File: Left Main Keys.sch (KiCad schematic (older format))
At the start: 6 parts

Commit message: Schematic completed first draft
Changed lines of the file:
@@
 $Descr A4 11693 8268
 encoding utf-8
-Sheet 9 12
+Sheet 11 18
 Title ""
 Date ""
@@
 Entry Wire Line
 	6150 6500 6250 6600
-Wire Bus Line
-	6350 6200 6250 6200
-Wire Bus Line
-	6350 6100 6250 6100
-Connection ~ 6350 6100
-Wire Bus Line
-	6350 6100 6350 6200
-Wire Bus Line
-	6350 6000 6250 6000
-Connection ~ 6350 6000
-Wire Bus Line
-	6350 6000 6350 6100
-Wire Bus Line
-	6350 5900 6250 5900
-Connection ~ 6350 5900
-Wire Bus Line
-	6350 5900 6350 6000
-Wire Bus Line
-	6350 5800 6250 5800
-Connection ~ 6350 5800
-Wire Bus Line
-	6350 5800 6350 5900
-Wire Bus Line
-	6350 5700 6250 5700
-Connection ~ 6350 5700
-Wire Bus Line
-	6350 5700 6350 5800
-Wire Bus Line
-	6350 5600 6250 5600
-Connection ~ 6350 5600
-Wire Bus Line
-	6350 5600 6350 5700
-Wire Bus Line
-	6350 5500 6250 5500
-Connection ~ 6350 5500
-Wire Bus Line
-	6350 5500 6350 5600
 Entry Wire Line
 	3200 2900 3300 2800
@@
 Entry Wire Line
 	7100 3200 7200 3100
-Wire Bus Line
-	6250 6300 6450 6300
-Wire Bus Line
-	6250 6400 6450 6400
-Wire Bus Line
-	6250 6500 6450 6500
-Wire Bus Line
-	6250 6600 6450 6600
-Connection ~ 6450 6300
-Connection ~ 6450 6400
-Wire Bus Line
-	6450 6400 6450 6300
-Connection ~ 6450 6500
-Wire Bus Line
-	6450 6500 6450 6400
-Wire Bus Line
-	6450 6600 6450 6500
 Text HLabel 10100 1150 0    50   Input ~ 0
 SHIFT_0_DATA_IN
 Wire Wire Line
 	10100 1150 10600 1150
-Wire Bus Line
-	6350 4300 6350 5500
 Wire Wire Line
 	1000 1150 1400 1150
@@
 Wire Wire Line
 	9350 1250 9350 3500
-Wire Bus Line
-	3200 4400 6250 4400
 Wire Wire Line
 	1500 1050 4100 1050
@@
 Wire Wire Line
 	8500 3500 9350 3500
-Wire Bus Line
-	6450 4300 6450 6300
 $Sheet
 S 4650 4550 1250 2050
@@
 Wire Wire Line
 	1500 4650 4650 4650
-Wire Bus Line
-	7100 4300 6450 4300
 Wire Wire Line
 	7200 2800 7400 2800
@@
 	5200 3500 5400 3500
 Wire Bus Line
-	5100 4300 6350 4300
-Wire Bus Line
-	7100 2900 7100 4300
-Wire Bus Line
-	5100 2900 5100 4300
-Wire Bus Line
-	3200 2900 3200 4400
-Wire Bus Line
-	6250 4400 6250 5400
+	6250 4350 5100 4350
+Connection ~ 5100 4350
+Wire Bus Line
+	5100 4350 3200 4350
+Wire Bus Line
+	6250 4350 7100 4350
+Wire Bus Line
+	7100 2900 7100 4350
+Wire Bus Line
+	3200 2900 3200 4350
+Wire Bus Line
+	5100 2900 5100 4350
+Wire Bus Line
+	6250 4350 6250 6600
+Connection ~ 6250 4350
 $EndSCHEMATC

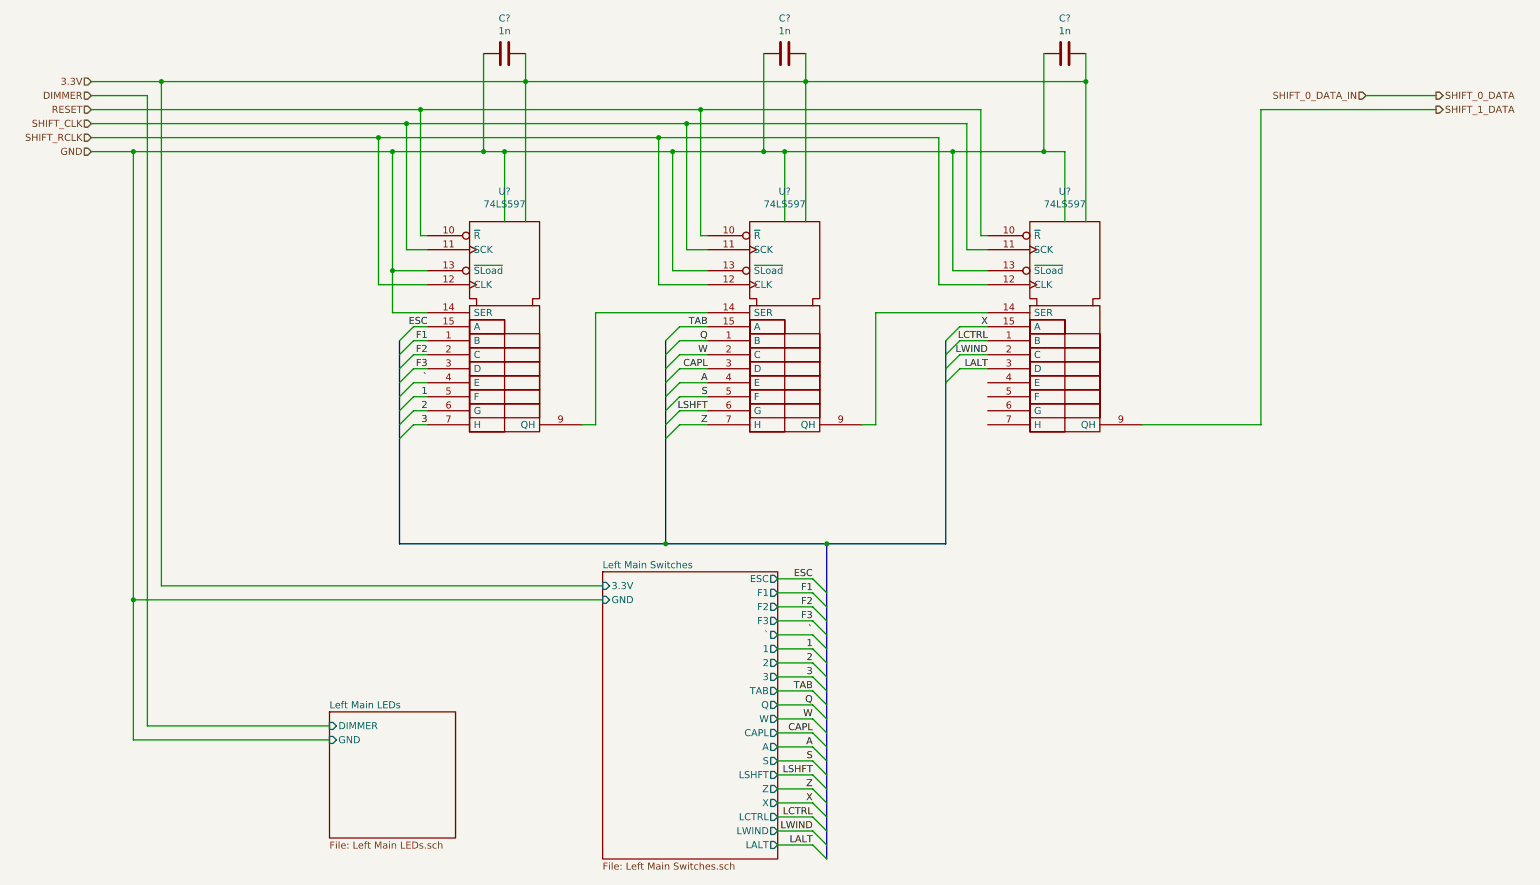
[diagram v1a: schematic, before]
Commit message: Fixed PISO Shift Register Wiring
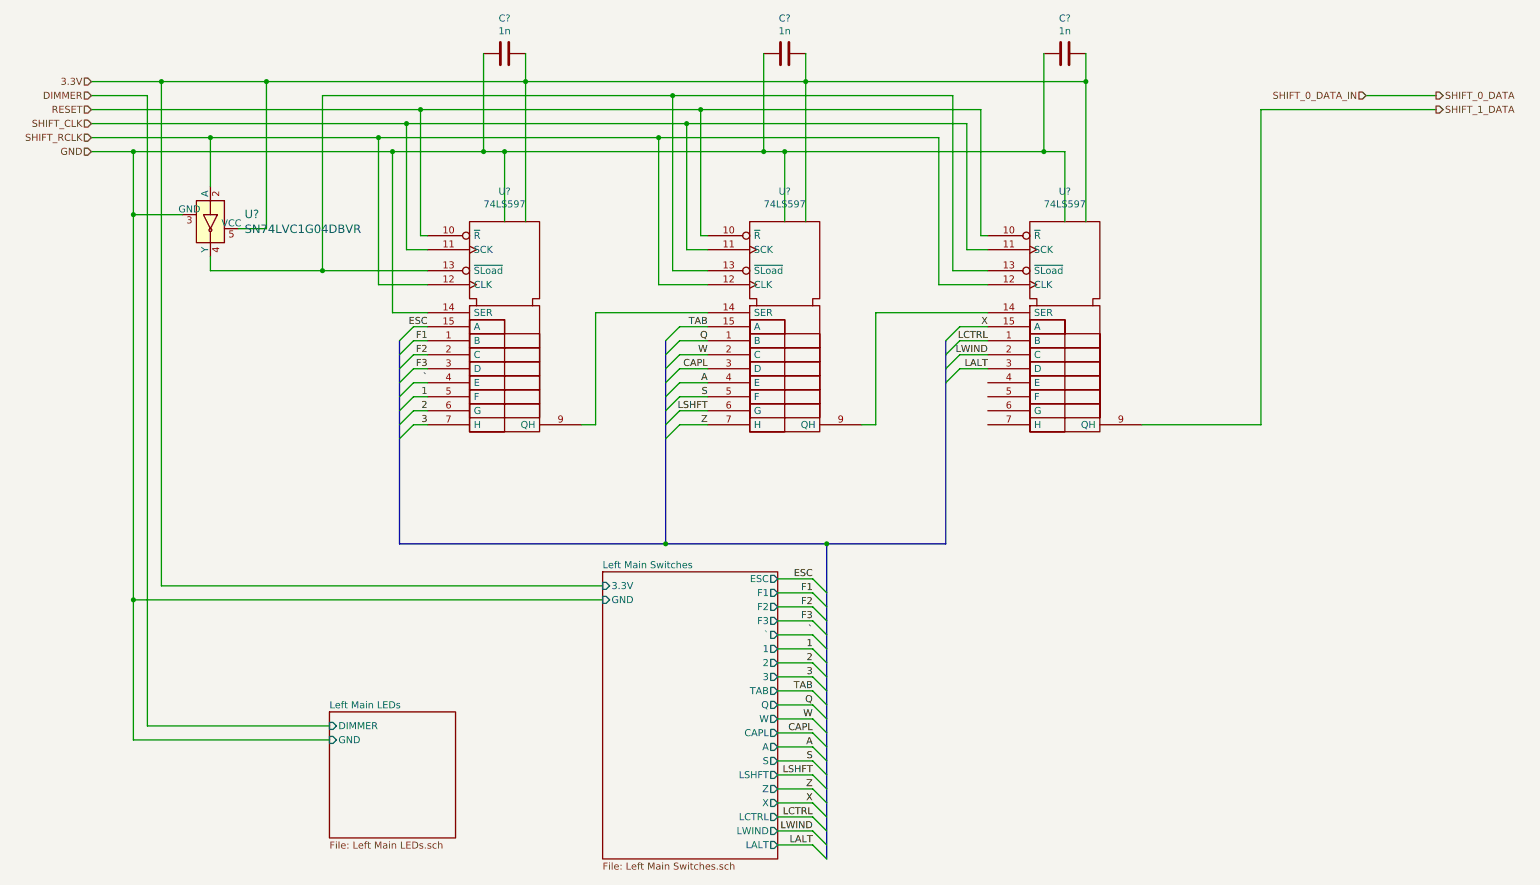
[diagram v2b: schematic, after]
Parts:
- added U?: SN74LVC1G04DBVR, digikey-footprints:SOT-753, symbol dk_Logic-Gates-and-Inverters:SN74LVC1G04DBVR
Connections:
- net GND: now also U?.3 (GND); no longer U?.13 (~SLoad), U?.13 (~SLoad), U?.13 (~SLoad)
- net SHIFT_RCLK: now also U?.2 (A)
- net VCC: now also U?.5 (VCC)
- new net: U?.13 (~SLoad), U?.13 (~SLoad), U?.13 (~SLoad), U?.4 (Y)
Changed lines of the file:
@@
 $Descr A4 11693 8268
 encoding utf-8
-Sheet 11 18
+Sheet 16 18
 Title ""
 Date ""
@@
 	3950 1550 3950 2050
 Wire Wire Line
-	3950 1550 5150 1550
-Wire Wire Line
 	5950 1550 5950 2050
 Connection ~ 3950 1550
@@
 Connection ~ 8100 1050
 Wire Wire Line
-	5950 1550 7150 1550
-Wire Wire Line
 	3350 1250 3350 2150
 Wire Wire Line
@@
 	7250 2250 7400 2250
 Connection ~ 5250 1350
-Wire Wire Line
-	3400 2400 3150 2400
-Wire Wire Line
-	3150 2400 3150 1550
 Connection ~ 3150 1550
 Wire Wire Line
@@
 Connection ~ 3050 1450
 Wire Wire Line
-	5400 2400 5150 2400
-Wire Wire Line
-	5150 2400 5150 1550
-Connection ~ 5150 1550
-Wire Wire Line
-	5150 1550 5800 1550
-Wire Wire Line
-	7400 2400 7150 2400
-Wire Wire Line
-	7150 2400 7150 1550
-Connection ~ 7150 1550
-Wire Wire Line
-	7150 1550 7800 1550
-Wire Wire Line
 	3050 1450 5050 1450
 Wire Wire Line
@@
 	5050 1450 7050 1450
 Wire Wire Line
-	3150 2400 3150 2700
-Wire Wire Line
 	3150 2700 3400 2700
-Connection ~ 3150 2400
 $Comp
 L Device:C C?
@@
 Wire Wire Line
 	9350 1250 9350 3500
-Wire Wire Line
-	1500 1050 4100 1050
 Connection ~ 1500 1050
 Wire Wire Line
@@
 Wire Wire Line
 	1000 1350 3250 1350
-Wire Wire Line
-	1000 1450 3050 1450
 Wire Wire Line
 	1300 1550 3150 1550
@@
 $EndSheet
 Wire Wire Line
-	1300 1550 1300 4750
-Wire Wire Line
 	4650 4750 1300 4750
 Connection ~ 1300 4750
@@
 Wire Bus Line
 	6250 4350 7100 4350
+Connection ~ 6250 4350
+Wire Wire Line
+	3150 1550 3150 2700
+Wire Wire Line
+	3950 1550 5800 1550
+Wire Wire Line
+	5950 1550 7800 1550
+Wire Wire Line
+	1300 1550 1300 2000
+$Comp
+L dk_Logic-Gates-and-Inverters:SN74LVC1G04DBVR U?
+U 1 1 5EC63679
+P 1850 2100
+F 0 "U?" V 1747 2344 60  0000 L CNN
+F 1 "SN74LVC1G04DBVR" V 1853 2344 60  0000 L CNN
+F 2 "digikey-footprints:SOT-753" H 2050 2300 60  0001 L CNN
+F 3 "http://www.ti.com/general/docs/suppproductinfo.tsp?distId=10&gotoUrl=http%3A%2F%2Fwww.ti.com%2Flit%2Fgpn%2Fsn74lvc1g04" H 2050 2400 60  0001 L CNN
+F 4 "296-11599-1-ND" H 2050 2500 60  0001 L CNN "Digi-Key_PN"
+F 5 "SN74LVC1G04DBVR" H 2050 2600 60  0001 L CNN "MPN"
+F 6 "Integrated Circuits (ICs)" H 2050 2700 60  0001 L CNN "Category"
+F 7 "Logic - Gates and Inverters" H 2050 2800 60  0001 L CNN "Family"
+F 8 "http://www.ti.com/general/docs/suppproductinfo.tsp?distId=10&gotoUrl=http%3A%2F%2Fwww.ti.com%2Flit%2Fgpn%2Fsn74lvc1g04" H 2050 2900 60  0001 L CNN "DK_Datasheet_Link"
+F 9 "/product-detail/en/texas-instruments/SN74LVC1G04DBVR/296-11599-1-ND/385738" H 2050 3000 60  0001 L CNN "DK_Detail_Page"
+F 10 "IC INVERTER 1CH 1-INP SOT23-5" H 2050 3100 60  0001 L CNN "Description"
+F 11 "Texas Instruments" H 2050 3200 60  0001 L CNN "Manufacturer"
+F 12 "Active" H 2050 3300 60  0001 L CNN "Status"
+	1    1850 2100
+	0    1    1    0
+$EndComp
+Wire Wire Line
+	1650 2000 1300 2000
+Wire Wire Line
+	1000 1450 1850 1450
+Wire Wire Line
+	1500 1050 2250 1050
+Connection ~ 1300 2000
+Wire Wire Line
+	1300 2000 1300 4750
+Wire Wire Line
+	1850 1800 1850 1450
+Connection ~ 1850 1450
+Wire Wire Line
+	1850 1450 3050 1450
+Wire Wire Line
+	2050 2100 2250 2100
+Wire Wire Line
+	2250 2100 2250 1050
+Connection ~ 2250 1050
+Wire Wire Line
+	2250 1050 4100 1050
+Wire Wire Line
+	1850 2300 1850 2400
+Wire Wire Line
+	1850 2400 2650 2400
+Wire Wire Line
+	2650 2400 2650 1150
+Wire Wire Line
+	2650 1150 5150 1150
+Wire Wire Line
+	5150 1150 5150 2400
+Wire Wire Line
+	5150 2400 5400 2400
+Connection ~ 2650 2400
+Wire Wire Line
+	2650 2400 3400 2400
+Wire Wire Line
+	5150 1150 7150 1150
+Wire Wire Line
+	7150 1150 7150 2400
+Wire Wire Line
+	7150 2400 7400 2400
+Connection ~ 5150 1150
 Wire Bus Line
 	7100 2900 7100 4350
 Wire Bus Line
+	5100 2900 5100 4350
+Wire Bus Line
 	3200 2900 3200 4350
 Wire Bus Line
-	5100 2900 5100 4350
-Wire Bus Line
 	6250 4350 6250 6600
-Connection ~ 6250 4350
 $EndSCHEMATC

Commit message: Corrected errors found in design rule check
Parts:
- C112, C113, C114: renamed from C?; footprint (none) -> Capacitor_SMD:C_1206_3216Metric_Pad1.42x1.75mm_HandSolder
- U21, U22, U23: renamed from U?; footprint (none) -> Package_SO:SOIC-16_3.9x9.9mm_P1.27mm
- gave numbers to parts that had none: 1
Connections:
- no-connect marks 0 -> 4
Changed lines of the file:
@@
 P 3950 2850
 AR Path="/5E8C77AE/5EAE0DF3" Ref="U?"  Part="1"
-AR Path="/5E8C755A/5EAE0DF3" Ref="U?"  Part="1"
-F 0 "U?" H 3950 3866 50  0000 C CNN
+AR Path="/5E8C755A/5EAE0DF3" Ref="U21"  Part="1"
+F 0 "U21" H 3950 3866 50  0000 C CNN
 F 1 "74LS597" H 3950 3775 50  0000 C CNN
-F 2 "" H 3950 2850 50  0001 C CNN
+F 2 "Package_SO:SOIC-16_3.9x9.9mm_P1.27mm" H 3950 2850 50  0001 C CNN
 F 3 "" H 3950 2850 50  0001 C CNN
 	1    3950 2850
@@
 P 5950 2850
 AR Path="/5E8C77AE/5EAE0DF9" Ref="U?"  Part="1"
-AR Path="/5E8C755A/5EAE0DF9" Ref="U?"  Part="1"
-F 0 "U?" H 5950 3866 50  0000 C CNN
+AR Path="/5E8C755A/5EAE0DF9" Ref="U22"  Part="1"
+F 0 "U22" H 5950 3866 50  0000 C CNN
 F 1 "74LS597" H 5950 3775 50  0000 C CNN
-F 2 "" H 5950 2850 50  0001 C CNN
+F 2 "Package_SO:SOIC-16_3.9x9.9mm_P1.27mm" H 5950 2850 50  0001 C CNN
 F 3 "" H 5950 2850 50  0001 C CNN
 	1    5950 2850
@@
 P 7950 2850
 AR Path="/5E8C77AE/5EAE0DFF" Ref="U?"  Part="1"
-AR Path="/5E8C755A/5EAE0DFF" Ref="U?"  Part="1"
-F 0 "U?" H 7950 3866 50  0000 C CNN
+AR Path="/5E8C755A/5EAE0DFF" Ref="U23"  Part="1"
+F 0 "U23" H 7950 3866 50  0000 C CNN
 F 1 "74LS597" H 7950 3775 50  0000 C CNN
-F 2 "" H 7950 2850 50  0001 C CNN
+F 2 "Package_SO:SOIC-16_3.9x9.9mm_P1.27mm" H 7950 2850 50  0001 C CNN
 F 3 "" H 7950 2850 50  0001 C CNN
 	1    7950 2850
@@
 P 3950 850
 AR Path="/5E8C77AE/5EAE0E47" Ref="C?"  Part="1"
-AR Path="/5E8C755A/5EAE0E47" Ref="C?"  Part="1"
-F 0 "C?" V 3698 850 50  0000 C CNN
+AR Path="/5E8C755A/5EAE0E47" Ref="C112"  Part="1"
+F 0 "C112" V 3698 850 50  0000 C CNN
 F 1 "1n" V 3789 850 50  0000 C CNN
-F 2 "" H 3988 700 50  0001 C CNN
+F 2 "Capacitor_SMD:C_1206_3216Metric_Pad1.42x1.75mm_HandSolder" H 3988 700 50  0001 C CNN
 F 3 "~" H 3950 850 50  0001 C CNN
 	1    3950 850
@@
 P 5950 850
 AR Path="/5E8C77AE/5EAE0E4D" Ref="C?"  Part="1"
-AR Path="/5E8C755A/5EAE0E4D" Ref="C?"  Part="1"
-F 0 "C?" V 5698 850 50  0000 C CNN
+AR Path="/5E8C755A/5EAE0E4D" Ref="C113"  Part="1"
+F 0 "C113" V 5698 850 50  0000 C CNN
 F 1 "1n" V 5789 850 50  0000 C CNN
-F 2 "" H 5988 700 50  0001 C CNN
+F 2 "Capacitor_SMD:C_1206_3216Metric_Pad1.42x1.75mm_HandSolder" H 5988 700 50  0001 C CNN
 F 3 "~" H 5950 850 50  0001 C CNN
 	1    5950 850
@@
 P 7950 850
 AR Path="/5E8C77AE/5EAE0E53" Ref="C?"  Part="1"
-AR Path="/5E8C755A/5EAE0E53" Ref="C?"  Part="1"
-F 0 "C?" V 7698 850 50  0000 C CNN
+AR Path="/5E8C755A/5EAE0E53" Ref="C114"  Part="1"
+F 0 "C114" V 7698 850 50  0000 C CNN
 F 1 "1n" V 7789 850 50  0000 C CNN
-F 2 "" H 7988 700 50  0001 C CNN
+F 2 "Capacitor_SMD:C_1206_3216Metric_Pad1.42x1.75mm_HandSolder" H 7988 700 50  0001 C CNN
 F 3 "~" H 7950 850 50  0001 C CNN
 	1    7950 850
@@
 	1300 1550 1300 2000
 $Comp
-L dk_Logic-Gates-and-Inverters:SN74LVC1G04DBVR U?
+L dk_Logic-Gates-and-Inverters:SN74LVC1G04DBVR U20
 U 1 1 5EC63679
 P 1850 2100
-F 0 "U?" V 1747 2344 60  0000 L CNN
+F 0 "U20" V 1747 2344 60  0000 L CNN
 F 1 "SN74LVC1G04DBVR" V 1853 2344 60  0000 L CNN
 F 2 "digikey-footprints:SOT-753" H 2050 2300 60  0001 L CNN
@@
 	7150 2400 7400 2400
 Connection ~ 5150 1150
+NoConn ~ 7400 3200
+NoConn ~ 7400 3300
+NoConn ~ 7400 3400
+NoConn ~ 7400 3500
 Wire Bus Line
 	7100 2900 7100 4350

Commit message: Redesigned for single large PCB
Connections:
- net labels removed: SHIFT_0_DATA, SHIFT_0_DATA_IN
- wire segments 129 -> 103
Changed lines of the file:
@@
 $Descr A4 11693 8268
 encoding utf-8
-Sheet 16 18
+Sheet 17 18
 Title ""
 Date ""
@@
 Text HLabel 1000 1550 0    50   Input ~ 0
 GND
-Text HLabel 10600 1150 2    50   Output ~ 0
-SHIFT_0_DATA
 Text HLabel 10600 1250 2    50   Output ~ 0
 SHIFT_1_DATA
@@
 Wire Wire Line
 	9350 1250 10600 1250
-Entry Wire Line
-	6150 4600 6250 4700
-Text Label 6150 4600 2    50   ~ 0
-ESC
-Text Label 6150 4700 2    50   ~ 0
-F1
-Text Label 6150 4800 2    50   ~ 0
-F2
-Text Label 6150 4900 2    50   ~ 0
-F3
-Text Label 6150 5000 2    50   ~ 0
-`
-Text Label 6150 5100 2    50   ~ 0
-1
-Text Label 6150 5200 2    50   ~ 0
-2
-Text Label 6150 5300 2    50   ~ 0
-3
-Text Label 6150 5400 2    50   ~ 0
-TAB
-Text Label 6150 5500 2    50   ~ 0
-Q
-Text Label 6150 5600 2    50   ~ 0
-W
-Text Label 6150 5700 2    50   ~ 0
-CAPL
-Text Label 6150 5800 2    50   ~ 0
-A
-Text Label 6150 5900 2    50   ~ 0
-S
-Text Label 6150 6000 2    50   ~ 0
-LSHFT
-Text Label 6150 6100 2    50   ~ 0
-Z
-Text Label 6150 6200 2    50   ~ 0
-X
-Text Label 6150 6300 2    50   ~ 0
-LCTRL
-Text Label 6150 6400 2    50   ~ 0
-LWIND
-Text Label 6150 6500 2    50   ~ 0
-LALT
-Entry Wire Line
-	6150 4700 6250 4800
-Entry Wire Line
-	6150 4800 6250 4900
-Entry Wire Line
-	6150 4900 6250 5000
-Entry Wire Line
-	6150 5000 6250 5100
-Entry Wire Line
-	6150 5100 6250 5200
-Entry Wire Line
-	6150 5200 6250 5300
-Entry Wire Line
-	6150 5300 6250 5400
 Wire Wire Line
 	3400 2800 3300 2800
@@
 LALT
 Entry Wire Line
-	6150 5400 6250 5500
-Entry Wire Line
-	6150 5500 6250 5600
-Entry Wire Line
-	6150 5600 6250 5700
-Entry Wire Line
-	6150 5700 6250 5800
-Entry Wire Line
-	6150 5800 6250 5900
-Entry Wire Line
-	6150 5900 6250 6000
-Entry Wire Line
-	6150 6000 6250 6100
-Entry Wire Line
-	6150 6100 6250 6200
-Entry Wire Line
-	6150 6200 6250 6300
-Entry Wire Line
-	6150 6300 6250 6400
-Entry Wire Line
-	6150 6400 6250 6500
-Entry Wire Line
-	6150 6500 6250 6600
-Entry Wire Line
 	3200 2900 3300 2800
 Entry Wire Line
@@
 Entry Wire Line
 	7100 3200 7200 3100
-Text HLabel 10100 1150 0    50   Input ~ 0
-SHIFT_0_DATA_IN
-Wire Wire Line
-	10100 1150 10600 1150
 Wire Wire Line
 	1000 1150 1400 1150
@@
 	1400 1150 1400 5650
 Wire Wire Line
-	1400 5650 2700 5650
-Wire Wire Line
 	1500 1050 1500 4650
-Wire Wire Line
-	1300 5750 2700 5750
 Wire Wire Line
 	9350 1250 9350 3500
@@
 Wire Wire Line
 	8500 3500 9350 3500
-$Sheet
-S 4650 4550 1250 2050
-U 5EAE0F3A
-F0 "Left Main Switches" 50
-F1 "Left Main Switches.sch" 50
-F2 "3.3V" I L 4650 4650 50
-F3 "GND" I L 4650 4750 50
-F4 "ESC" O R 5900 4600 50
-F5 "F1" O R 5900 4700 50
-F6 "F2" O R 5900 4800 50
-F7 "F3" O R 5900 4900 50
-F8 "`" O R 5900 5000 50
-F9 "1" O R 5900 5100 50
-F10 "2" O R 5900 5200 50
-F11 "3" O R 5900 5300 50
-F12 "TAB" O R 5900 5400 50
-F13 "Q" O R 5900 5500 50
-F14 "W" O R 5900 5600 50
-F15 "CAPL" O R 5900 5700 50
-F16 "A" O R 5900 5800 50
-F17 "S" O R 5900 5900 50
-F18 "Z" O R 5900 6100 50
-F19 "X" O R 5900 6200 50
-F20 "LALT" O R 5900 6500 50
-F21 "LSHFT" O R 5900 6000 50
-F22 "LCTRL" O R 5900 6300 50
-F23 "LWIND" O R 5900 6400 50
-$EndSheet
-Wire Wire Line
-	4650 4750 1300 4750
-Connection ~ 1300 4750
-Wire Wire Line
-	1300 4750 1300 5750
-$Sheet
-S 2700 5550 900  900
-U 5FA6DC21
-F0 "Left Main LEDs" 50
-F1 "Left Main LEDs.sch" 50
-F2 "DIMMER" I L 2700 5650 50
-F3 "GND" I L 2700 5750 50
-$EndSheet
-Wire Wire Line
-	5900 4600 6150 4600
-Wire Wire Line
-	5900 4700 6150 4700
-Wire Wire Line
-	5900 4800 6150 4800
-Wire Wire Line
-	5900 4900 6150 4900
-Wire Wire Line
-	5900 5000 6150 5000
-Wire Wire Line
-	5900 5100 6150 5100
-Wire Wire Line
-	5900 5200 6150 5200
-Wire Wire Line
-	5900 5300 6150 5300
-Wire Wire Line
-	5900 5400 6150 5400
-Wire Wire Line
-	5900 5500 6150 5500
-Wire Wire Line
-	5900 5600 6150 5600
-Wire Wire Line
-	5900 5700 6150 5700
-Wire Wire Line
-	5900 5800 6150 5800
-Wire Wire Line
-	5900 5900 6150 5900
-Wire Wire Line
-	5900 6000 6150 6000
-Wire Wire Line
-	5900 6100 6150 6100
-Wire Wire Line
-	5900 6200 6150 6200
-Wire Wire Line
-	5900 6300 6150 6300
-Wire Wire Line
-	5900 6400 6150 6400
-Wire Wire Line
-	5900 6500 6150 6500
-Wire Wire Line
-	1500 4650 4650 4650
 Wire Wire Line
 	7200 2800 7400 2800
@@
 Wire Wire Line
 	5200 3500 5400 3500
-Wire Bus Line
-	6250 4350 5100 4350
 Connection ~ 5100 4350
 Wire Bus Line
 	5100 4350 3200 4350
-Wire Bus Line
-	6250 4350 7100 4350
-Connection ~ 6250 4350
 Wire Wire Line
 	3150 1550 3150 2700
@@
 Connection ~ 1300 2000
 Wire Wire Line
-	1300 2000 1300 4750
-Wire Wire Line
 	1850 1800 1850 1450
 Connection ~ 1850 1450
@@
 NoConn ~ 7400 3400
 NoConn ~ 7400 3500
+Wire Wire Line
+	1300 2000 1300 5750
+Wire Bus Line
+	5100 4350 7100 4350
 Wire Bus Line
 	7100 2900 7100 4350
@@
 Wire Bus Line
 	3200 2900 3200 4350
-Wire Bus Line
-	6250 4350 6250 6600
 $EndSCHEMATC
